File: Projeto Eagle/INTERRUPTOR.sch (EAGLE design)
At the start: 5 parts, among them J1 CONECTOR, J2 CONECTOR, U1 74HC132

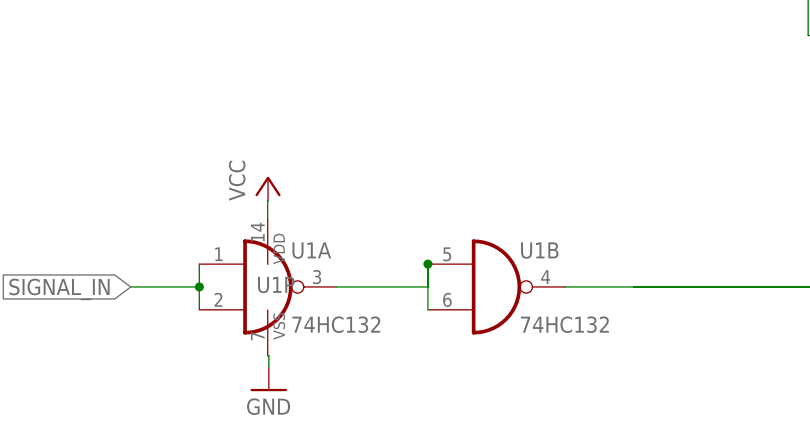
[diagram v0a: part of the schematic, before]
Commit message: correção de pads, adição de label para versionamento e plano de VCC
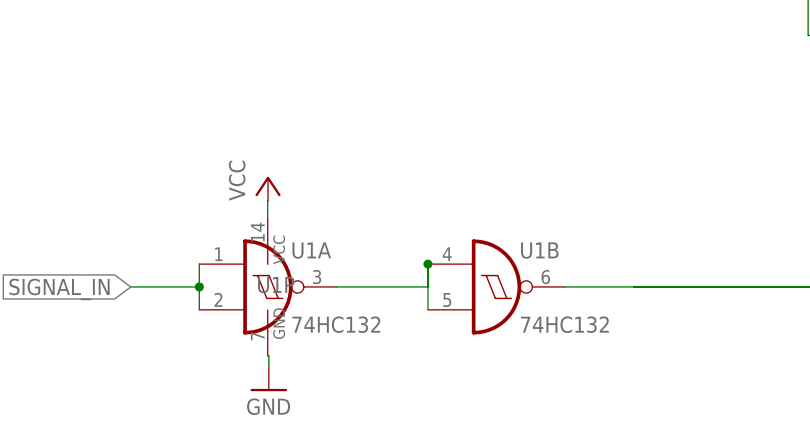
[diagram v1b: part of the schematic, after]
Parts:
- J1: value CONECTOR -> CONECTOR_MACHO; device Eletroblocks Lib:CONECTOR -> Eletroblocks Lib:CONECTOR_MACHO
- J2: value CONECTOR -> CONECTOR_FEMEA; device Eletroblocks Lib:CONECTOR -> Eletroblocks Lib:CONECTOR_FEMEA
- U1: device 40xx:4011D -> 74xx-eu:74HC132D
- renumbered U$1 to J3
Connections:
- net GND: now also U1P.GND; no longer U1P.VSS
- net VCC: now also U1P.VCC; no longer U1P.VDD
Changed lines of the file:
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@@
 <part name="P+4" library="supply1" library_urn="urn:adsk.eagle:library:371" deviceset="VCC" device=""/>
 <part name="GND2" library="supply1" library_urn="urn:adsk.eagle:library:371" deviceset="GND" device=""/>
-<part name="J1" library="Eletroblocks Lib" deviceset="CONECTOR" device="" override_package3d_urn="urn:adsk.eagle:package:23099674/4" override_package_urn="urn:adsk.eagle:footprint:23099675/1"/>
-<part name="J2" library="Eletroblocks Lib" deviceset="CONECTOR" device="" override_package3d_urn="urn:adsk.eagle:package:23099664/2" override_package_urn="urn:adsk.eagle:footprint:23099665/1"/>
-<part name="U$1" library="Eletroblocks Lib" deviceset="SS12F46" device=""/>
+<part name="J1" library="Eletroblocks Lib" deviceset="CONECTOR_MACHO" device="" override_package3d_urn="urn:adsk.eagle:package:23099674/4" override_package_urn="urn:adsk.eagle:footprint:23099675/1" override_locally_modified="yes"/>
+<part name="J2" library="Eletroblocks Lib" deviceset="CONECTOR_FEMEA" device="" override_package3d_urn="urn:adsk.eagle:package:23099664/2" override_package_urn="urn:adsk.eagle:footprint:23099665/1" override_locally_modified="yes"/>
+<part name="J3" library="Eletroblocks Lib" deviceset="SS12F46" device=""/>
 <part name="GND7" library="supply1" library_urn="urn:adsk.eagle:library:371" deviceset="GND" device=""/>
-<part name="U1" library="40xx" library_urn="urn:adsk.eagle:library:80" deviceset="4011" device="D" package3d_urn="urn:adsk.eagle:package:823/2" value="74HC132"/>
+<part name="U1" library="74xx-eu" library_urn="urn:adsk.eagle:library:85" deviceset="74*132" device="D" package3d_urn="urn:adsk.eagle:package:1010/2" technology="HC" value="74HC132"/>
 <part name="P+7" library="supply1" library_urn="urn:adsk.eagle:library:371" deviceset="VCC" device=""/>
 <part name="GND8" library="supply1" library_urn="urn:adsk.eagle:library:371" deviceset="GND" device=""/>
@@
 <attribute name="NAME" x="35.8" y="242.18" size="1.778" layer="95"/>
 </instance>
-<instance part="U$1" gate="G$1" x="91.44" y="193.04" smashed="yes" rot="R270" grouprefs="CHAVE1"/>
+<instance part="J3" gate="G$1" x="91.44" y="193.04" smashed="yes" rot="R270" grouprefs="CHAVE1"/>
 <instance part="GND7" gate="1" x="87.97" y="204.036" smashed="yes" rot="R180" grouprefs="CHAVE1">
 <attribute name="VALUE" x="90.51" y="206.776" size="1.778" layer="96" rot="R180"/>
@@
 <segment>
 <pinref part="GND7" gate="1" pin="GND"/>
-<pinref part="U$1" gate="G$1" pin="P$1"/>
+<pinref part="J3" gate="G$1" pin="P$1"/>
 <wire x1="87.97" y1="201.496" x2="87.97" y2="193.04" width="0.1524" layer="91"/>
 <wire x1="87.97" y1="193.04" x2="91.44" y2="193.04" width="0.1524" layer="91"/>
@@
 <segment>
 <pinref part="GND8" gate="1" pin="GND"/>
-<pinref part="U1" gate="P" pin="VSS"/>
+<pinref part="U1" gate="P" pin="GND"/>
 <wire x1="28.04" y1="156.19" x2="28.04" y2="157.46" width="0.1524" layer="91" grouprefs="CHAVE1"/>
 <wire x1="28.04" y1="157.46" x2="27.92" y2="157.46" width="0.1524" layer="91" grouprefs="CHAVE1"/>
@@
 </segment>
 <segment>
-<pinref part="U$1" gate="G$1" pin="P$2"/>
+<pinref part="J3" gate="G$1" pin="P$2"/>
 <wire x1="104.14" y1="185.42" x2="116.84" y2="185.42" width="0.1524" layer="91" grouprefs="CHAVE1"/>
 <label x="116.84" y="185.42" size="1.778" layer="95" xref="yes" grouprefs="CHAVE1"/>
@@
 </segment>
 <segment>
-<pinref part="U1" gate="P" pin="VDD"/>
+<pinref part="U1" gate="P" pin="VCC"/>
 <pinref part="P+7" gate="VCC" pin="VCC"/>
 <wire x1="27.92" y1="172.7" x2="27.92" y2="174.674" width="0.1524" layer="91" grouprefs="CHAVE1"/>
@@
 <net name="N$3" class="0">
 <segment>
-<pinref part="U$1" gate="G$1" pin="P$3"/>
+<pinref part="J3" gate="G$1" pin="P$3"/>
 <pinref part="U1" gate="B" pin="O"/>
 <wire x1="60.96" y1="165.1" x2="91.44" y2="165.1" width="0.1524" layer="91" grouprefs="CHAVE1"/>
